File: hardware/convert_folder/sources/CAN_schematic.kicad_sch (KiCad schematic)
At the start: 12 parts, among them U23 SN65HVD232D, U24 SN65HVD232D

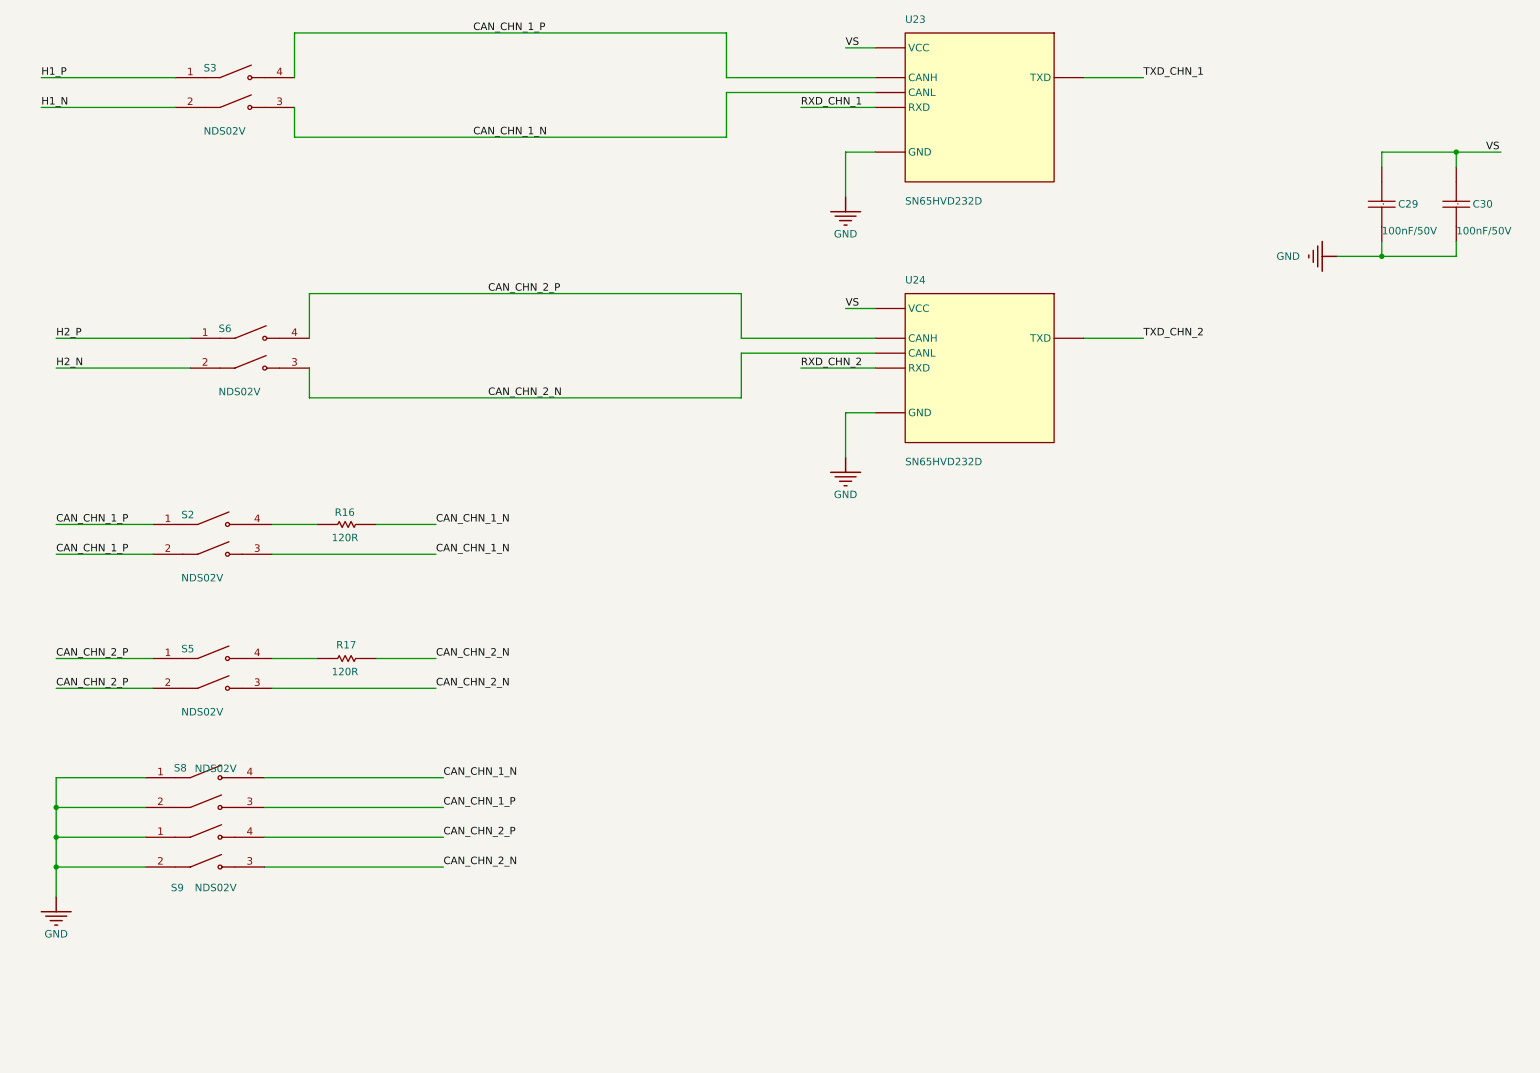
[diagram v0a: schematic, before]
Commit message: fix: fix a lot of connections between blocks. Many more to go...
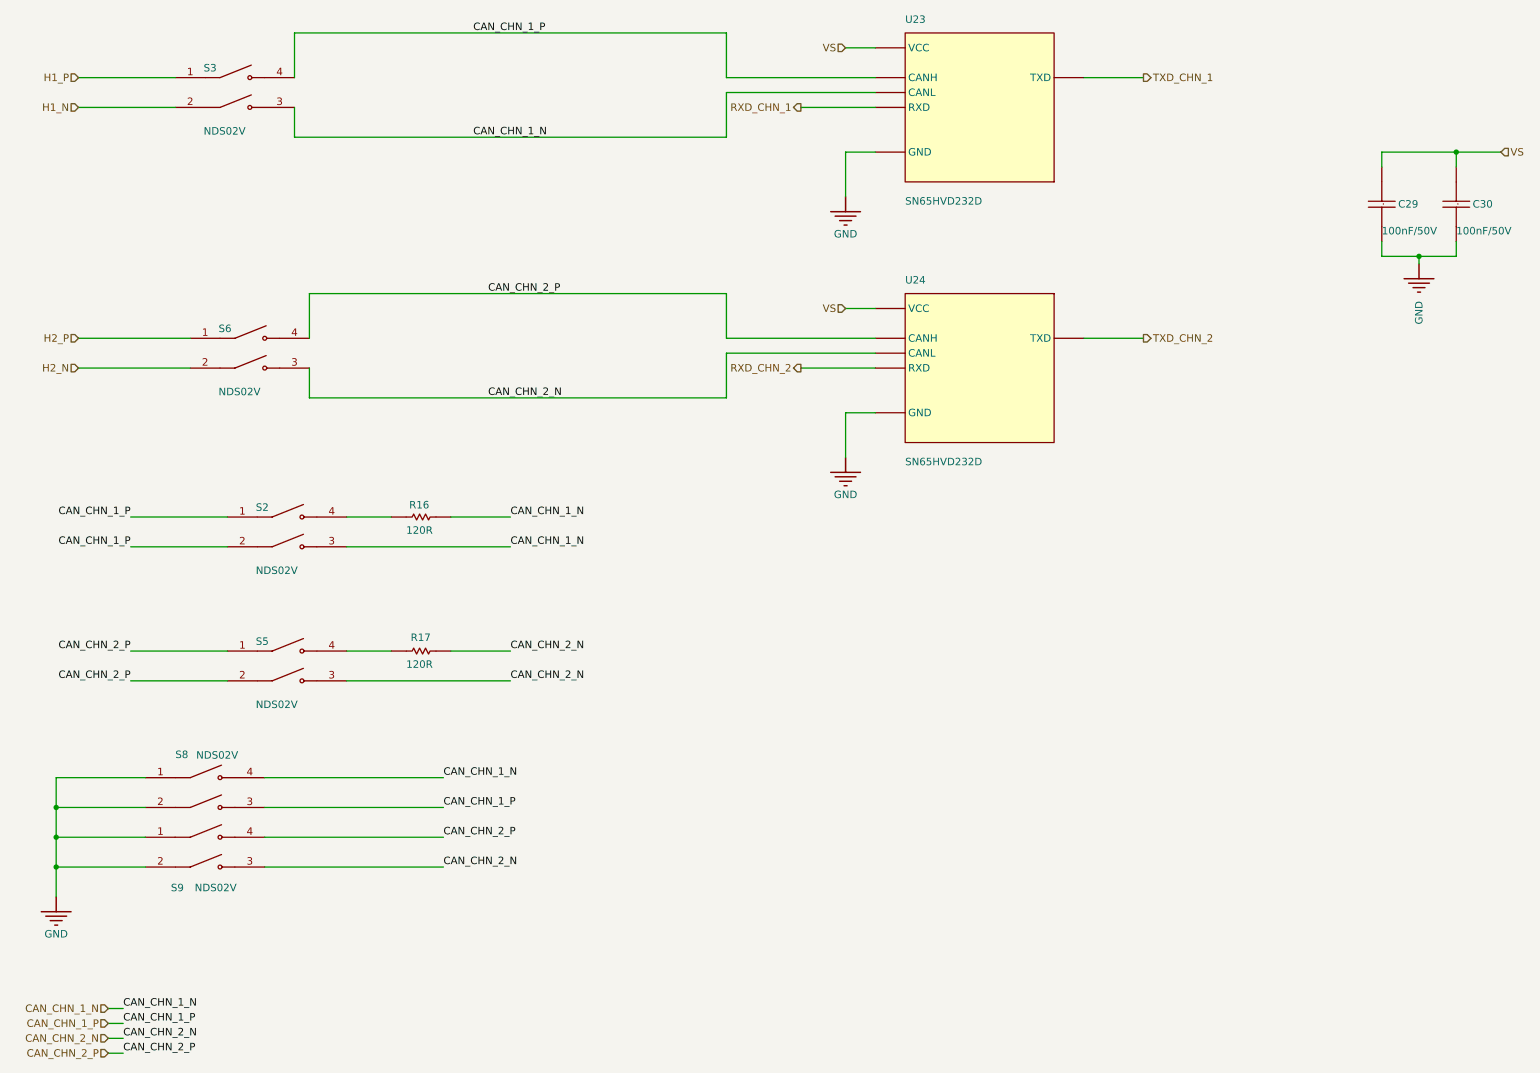
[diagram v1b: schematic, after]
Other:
- moved on the sheet: R16, R17, S2, S5

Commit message: fix: convert 90% of the schematic (there are 21 warnings/errors to resolve)
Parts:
- removed S2, S5, S8, S9: NDS02V, C__Users_icaro_Documents_AltiumLL_SamacSys.PcbLib:NDS02V, symbol SamacSys:root_0_NDS02V_SamacSys.SchLib
- removed U23, U24: SN65HVD232D, SOIC127P599X175-8N, symbol flatsat_platform_2:root_0_mirrored_SN65HVD232D_flatsat_platform_2.SchLib
- added S2, S5, S8, S9: NDS02V, altium_import:NDS02V, symbol altium_import:root_0_NDS02V_SamacSys.SchLib_alt
- added U23, U24: SN65HVD232D, altium_import:SN65HVD232D, symbol altium_import:root_0_mirrored_SN65HVD232D_flatsat_platform_2.SchLib
- C29, C30: footprint CC0603 -> altium_import:CC0603; symbol flatsat_platform_2:root_0_Cap_Cer_X7R_100nF_50V_0603_flatsat_platform_2.SchLib -> altium_import:root_0_Cap_Cer_X7R_100nF_50V_0603_flatsat_platform_2.SchLib
- R16, R17: footprint 0805 -> altium_import:0805; symbol flatsat_platform_2:root_1_R120R_1%_1/4W_0805_flatsat_platform_2.SchLib -> altium_import:root_1_R120R_1%_1/4W_0805_flatsat_platform_2.SchLib
- S3, S6: footprint C__Users_icaro_Documents_AltiumLL_SamacSys.PcbLib:NDS02V -> altium_import:NDS02V; symbol SamacSys:root_0_NDS02V_SamacSys.SchLib -> altium_import:root_0_NDS02V_SamacSys.SchLib
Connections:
- net CAN_CHN_1_N: now also S2.3 (NO_1), S8.4 (NO_2), U23.6 (CANL)
- net CAN_CHN_1_P: now also S2.1 (COM_1), S2.2 (COM_2), S8.3 (NO_1), U23.7 (CANH)
- net CAN_CHN_2_N: now also S5.3 (NO_1), S9.3 (NO_1), U24.6 (CANL)
- net CAN_CHN_2_P: now also S5.1 (COM_1), S5.2 (COM_2), S9.4 (NO_2), U24.7 (CANH)
- net GND: now also S8.1 (COM_1), S8.2 (COM_2), S9.1 (COM_1), S9.2 (COM_2), U23.2 (GND), U24.2 (GND)
- net RXD_CHN_1: now also U23.4 (RXD)
- net RXD_CHN_2: now also U24.4 (RXD)
- net TXD_CHN_1: now also U23.1 (TXD)
- net TXD_CHN_2: now also U24.1 (TXD)
- net VS: now also U23.3 (VCC), U24.3 (VCC)
- net at R17.2: now also S5.4 (NO_2)
- net at R16.2: now also S2.4 (NO_2)
